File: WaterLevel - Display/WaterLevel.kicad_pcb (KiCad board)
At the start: 2 copper layers, 58 parts, among them P1 PWR_SW, P2 PROBE, P3 AC 12V, P4 PUMP, P5 ALARM, Q1 2N2222, Q2 2N2222, U1 LM324N, U2 LM7812CT, U3 LM324N, U4 LM324N

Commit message: Display
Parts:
- removed C1: CP, Capacitors_ThroughHole:C_Radial_D5_L11_P2.5
- removed C2: CP, Capacitors_ThroughHole:C_Axial_D13_L31_P38
- removed D10: LN1, LEDs:LED-5MM
- removed D11: LN2, LEDs:LED-5MM
- removed D12: LN3, LEDs:LED-5MM
- removed D13: LN4, LEDs:LED-5MM
- removed D14: LN5, LEDs:LED-5MM
- removed D15: LN6, LEDs:LED-5MM
- removed D16: LN7, LEDs:LED-5MM
- removed D17: LN8, LEDs:LED-5MM
- removed D9: ALRM_LED, LEDs:LED-5MM
- removed F1: FUSE, Fuse_Holders_and_Fuses:Fuseholder5x20_horiz_open_Schurter_0031_8201
- removed P2: PROBE, Sockets_MOLEX_KK-System:Socket_MOLEX-KK-RM3-96mm_Lock_3pin_straight
- removed P3: AC 12V, Sockets_MOLEX_KK-System:Socket_MOLEX-KK-RM3-96mm_Lock_2pin_straight
- removed P4: PUMP, Sockets_MOLEX_KK-System:Socket_MOLEX-KK-RM3-96mm_Lock_2pin_straight
- removed P5: ALARM, Sockets_MOLEX_KK-System:Socket_MOLEX-KK-RM3-96mm_Lock_3pin_straight
- removed Q1, Q2: 2N2222, TO_SOT_Packages_THT:TO-18_3Pin
- removed R16, R17, R18, R19, R20: R, Resistors_ThroughHole:Resistor_Horizontal_RM7mm
- removed RL1, RL2: 12V/2A, Relays_ThroughHole:Relay_SPDT_Schrack-RT1_RM5mm
- removed RV3: ALRM_LVL, Potentiometers:Potentiometer_Trimmer-Piher_PT15-V15_horizontal
- removed RV4: LVL, Potentiometers:Potentiometer_Trimmer-Piher_PT15-V15_horizontal
- removed RV5: LVH, Potentiometers:Potentiometer_Trimmer-Piher_PT15-V15_horizontal
- removed U3, U4: LM324N, Housings_DIP:DIP-14_W7.62mm_LongPads
- D1: value 1N4007 -> LN1; footprint Diodes_ThroughHole:Diode_DO-41_SOD81_Vertical_KathodeUp -> LEDs:LED-5MM
- D2: value PUMP_LED -> LN2
- D3: value D -> LN3; footprint Diodes_ThroughHole:Diode_DO-41_SOD81_Vertical_KathodeUp -> LEDs:LED-5MM
- D4: value D -> LN4; footprint Diodes_ThroughHole:Diode_DO-41_SOD81_Vertical_KathodeUp -> LEDs:LED-5MM
- D5: value D -> LN5; footprint Diodes_ThroughHole:Diode_DO-41_SOD81_Vertical_KathodeUp -> LEDs:LED-5MM
- D6: value D -> LN6; footprint Diodes_ThroughHole:Diode_DO-41_SOD81_Vertical_KathodeUp -> LEDs:LED-5MM
- D7: value PWR_LED -> LN7
- D8: value 1N4007 -> LN8; footprint Diodes_ThroughHole:Diode_DO-41_SOD81_Vertical_KathodeUp -> LEDs:LED-5MM
- P1: value PWR_SW -> DISPLAY; footprint Sockets_MOLEX_KK-System:Socket_MOLEX-KK-RM3-96mm_Lock_2pin_straight -> Sockets_MOLEX_KK-System:Socket_MOLEX-KK-RM2-54mm_Lock_3pin_straight
- RV1: value POT -> LVL
- RV2: value POT -> LVH
- U2: value LM7812CT -> LM324N; footprint Power_Integrations:TO-220 -> Housings_DIP:DIP-14_W7.62mm_LongPads
- moved D6 117.4 mm to (151.9, 148.8), turned to 270 degrees
- moved D5 109.5 mm to (145.8, 148.8), turned to 270 degrees
- moved D1 106.5 mm to (120.9, 148.8)
- moved P1 100.1 mm to (162.1, 115.6), turned to 90 degrees
- moved D2 99.4 mm to (127.5, 148.8), turned to 270 degrees
- moved D4 98.4 mm to (139.7, 148.8), turned to 270 degrees
- moved R1 95.1 mm to (118.6, 131.6), turned to 180 degrees
- moved D3 90.4 mm to (133.6, 148.8), turned to 270 degrees
- moved R6 83.3 mm to (156.7, 128.5), turned to 180 degrees
- moved D7 78.8 mm to (158.0, 148.8), turned to 270 degrees
- moved R13 77.2 mm to (151.9, 137.9)
- moved R14 76.9 mm to (158.0, 137.9)
- moved R15 76.7 mm to (164.1, 137.9)
- moved R3 71.9 mm to (133.9, 131.6), turned to 180 degrees
- moved RV1 69.2 mm to (104.4, 151.4), turned to 0 degrees
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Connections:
- D1 pad 1: +12V -> Net-(D1-Pad1)
- D1 pad 2: Net-(D1-Pad2) -> +12V
- D2 pad 1: Net-(D1-Pad2) -> Net-(D2-Pad1)
- D2 pad 2: Net-(D2-Pad2) -> +12V
- D3 pad 2: Net-(D3-Pad2) -> +12V
- D4 pad 1: Net-(D3-Pad1) -> Net-(D4-Pad1)
- D4 pad 2: Net-(D4-Pad2) -> +12V
- D5 pad 1: GNDPWR -> Net-(D5-Pad1)
- D5 pad 2: Net-(D3-Pad2) -> +12V
- D6 pad 1: GNDPWR -> Net-(D6-Pad1)
- D6 pad 2: Net-(D4-Pad2) -> +12V
- D7 pad 1: GNDPWR -> Net-(D7-Pad1)
- D7 pad 2: Net-(D7-Pad2) -> +12V
- D8 pad 1: +12V -> Net-(D8-Pad1)
- D8 pad 2: Net-(D8-Pad2) -> +12V
- P1 pad 1: Net-(D3-Pad1) -> +12V
- P1 pad 2: +12VA -> Net-(P1-Pad2)
- R1 pad 1: +12V -> Net-(R1-Pad1)
- R1 pad 2: Net-(D2-Pad2) -> Net-(R1-Pad2)
- R10 pad 2: Net-(R10-Pad2) -> Net-(D3-Pad1)
- R11 pad 2: Net-(R10-Pad1) -> Net-(D4-Pad1)
- R12 pad 2: Net-(R11-Pad1) -> Net-(D5-Pad1)
- R13 pad 2: Net-(D10-Pad1) -> Net-(D6-Pad1)
- R14 pad 2: Net-(D11-Pad1) -> Net-(D7-Pad1)
- R15 pad 2: Net-(D12-Pad1) -> Net-(D8-Pad1)
- R2 pad 1: +12V -> Net-(R2-Pad1)
- R2 pad 2: Net-(D7-Pad2) -> Net-(R1-Pad1)
- R3 pad 2: Net-(Q1-Pad2) -> Net-(R2-Pad1)
- R4 pad 1: +12V -> Net-(R4-Pad1)
- R4 pad 2: Net-(D9-Pad2) -> Net-(R3-Pad1)
- R5 pad 2: Net-(Q2-Pad2) -> Net-(R4-Pad1)
- R6 pad 2: Net-(R6-Pad2) -> Net-(R5-Pad1)
- R8 pad 2: Net-(R7-Pad1) -> Net-(D1-Pad1)
- R9 pad 1: Net-(R10-Pad2) -> Net-(R9-Pad1)
- R9 pad 2: Net-(R8-Pad1) -> Net-(D2-Pad1)
- RV1 pad 1: +12V -> Net-(R1-Pad2)
- RV1 pad 2: Net-(RV1-Pad2) -> Net-(R1-Pad2)
- RV2 pad 1: VProbe -> +12V
- RV2 pad 2: Net-(RV2-Pad2) -> +12V
- RV2 pad 3: Net-(R3-Pad1) -> Net-(R7-Pad1)
- U1 pad 1: Net-(R3-Pad1) -> Net-(R8-Pad1)
- U1 pad 10: (no net) -> Net-(R2-Pad1)
- U1 pad 11: GNDPWR -> +12V
- U1 pad 12: (no net) -> Net-(R3-Pad1)
- U1 pad 13: (no net) -> Net-(P1-Pad2)
- U1 pad 14: (no net) -> Net-(R11-Pad1)
- U1 pad 2: Net-(RV1-Pad2) -> Net-(P1-Pad2)
- U1 pad 3: Net-(RV2-Pad2) -> Net-(R1-Pad2)
- U1 pad 4: +12V -> GNDPWR
- U1 pad 5: VProbe -> Net-(R1-Pad1)
- U1 pad 6: Net-(RV3-Pad2) -> Net-(P1-Pad2)
- U1 pad 7: Net-(R5-Pad1) -> Net-(R9-Pad1)
- U1 pad 8: (no net) -> Net-(R10-Pad1)
- U1 pad 9: (no net) -> Net-(P1-Pad2)
- U2 pad 1: +12VA -> Net-(R12-Pad1)
- U2 pad 2: GNDPWR -> Net-(P1-Pad2)
- U2 pad 3: +12V -> Net-(R4-Pad1)
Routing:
- net +12V: track 0.00 -> 169.2 mm
- net GNDPWR: track 0.00 -> 141.8 mm
- net Net-(R1-Pad2): track 0.00 -> 56.1 mm
- net Net-(R11-Pad1): track 0.00 -> 37.8 mm
- net Net-(R10-Pad1): track 0.00 -> 19.5 mm
- net Net-(R9-Pad1): track 0.00 -> 18.4 mm
- net Net-(R2-Pad1): track 0.00 -> 3.56 mm
- net Net-(D8-Pad1): track 0.00 -> 3.30 mm
- net Net-(D7-Pad1): track 0.00 -> 3.30 mm
- net Net-(D6-Pad1): track 0.00 -> 3.30 mm
- net Net-(D5-Pad1): track 0.00 -> 3.30 mm
- net Net-(D4-Pad1): track 0.00 -> 3.30 mm
- net Net-(D3-Pad1): track 0.00 -> 3.30 mm
- net Net-(D2-Pad1): track 0.00 -> 3.30 mm
- net Net-(D1-Pad1): track 0.00 -> 3.30 mm
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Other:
- net class Default: trace_width 0.25 -> 1

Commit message: PCB changes
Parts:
- moved RV2 3.09 mm to (104.4, 121.7)
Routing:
- net Net-(R8-Pad1): track 0.00 -> 37.3 mm, vias 0 -> 2
- net Net-(R12-Pad1): track 0.00 -> 36.5 mm, vias 0 -> 2
- net +12V: track 169.2 -> 202.3 mm
- net Net-(R1-Pad1): track 1.78 -> 24.1 mm, vias 0 -> 2
- net Net-(R3-Pad1): track 3.05 -> 25.2 mm
- net Net-(R4-Pad1): track 3.05 -> 24.9 mm
- net Net-(R14-Pad1): track 0.00 -> 20.8 mm
- net Net-(R13-Pad1): track 0.00 -> 20.8 mm
- net Net-(R2-Pad1): track 3.56 -> 20.4 mm
- net Net-(R5-Pad1): track 3.05 -> 18.5 mm
- net Net-(R6-Pad1): track 3.05 -> 18.4 mm
- net Net-(R11-Pad1): track 37.8 -> 35.6 mm
- net Net-(R9-Pad1): track 18.4 -> 20.5 mm
- net Net-(R1-Pad2): track 56.1 -> 58.0 mm
- net Net-(R10-Pad1): track 19.5 -> 20.1 mm
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
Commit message: Updates
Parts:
- added P2: VIN, Wire_Pads:SolderWirePad_single_1mmDrill, F.Cu at (166.8, 109.5)
- added P3: +12V, Wire_Pads:SolderWirePad_single_1mmDrill, F.Cu at (167.0, 102.0)
- P1: value DISPLAY -> GND; footprint Sockets_MOLEX_KK-System:Socket_MOLEX-KK-RM2-54mm_Lock_3pin_straight -> Wire_Pads:SolderWirePad_single_1mmDrill
- moved P1 5.24 mm to (166.8, 113.2)
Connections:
- P1 pad 1: +12V -> GNDPWR
- U1 pad 13: Net-(P1-Pad2) -> Net-(P2-Pad1)
- U1 pad 2: Net-(P1-Pad2) -> Net-(P2-Pad1)
- U1 pad 6: Net-(P1-Pad2) -> Net-(P2-Pad1)
- U1 pad 9: Net-(P1-Pad2) -> Net-(P2-Pad1)
- U2 pad 13: Net-(P1-Pad2) -> Net-(P2-Pad1)
- U2 pad 2: Net-(P1-Pad2) -> Net-(P2-Pad1)
- U2 pad 6: Net-(P1-Pad2) -> Net-(P2-Pad1)
- U2 pad 9: Net-(P1-Pad2) -> Net-(P2-Pad1)

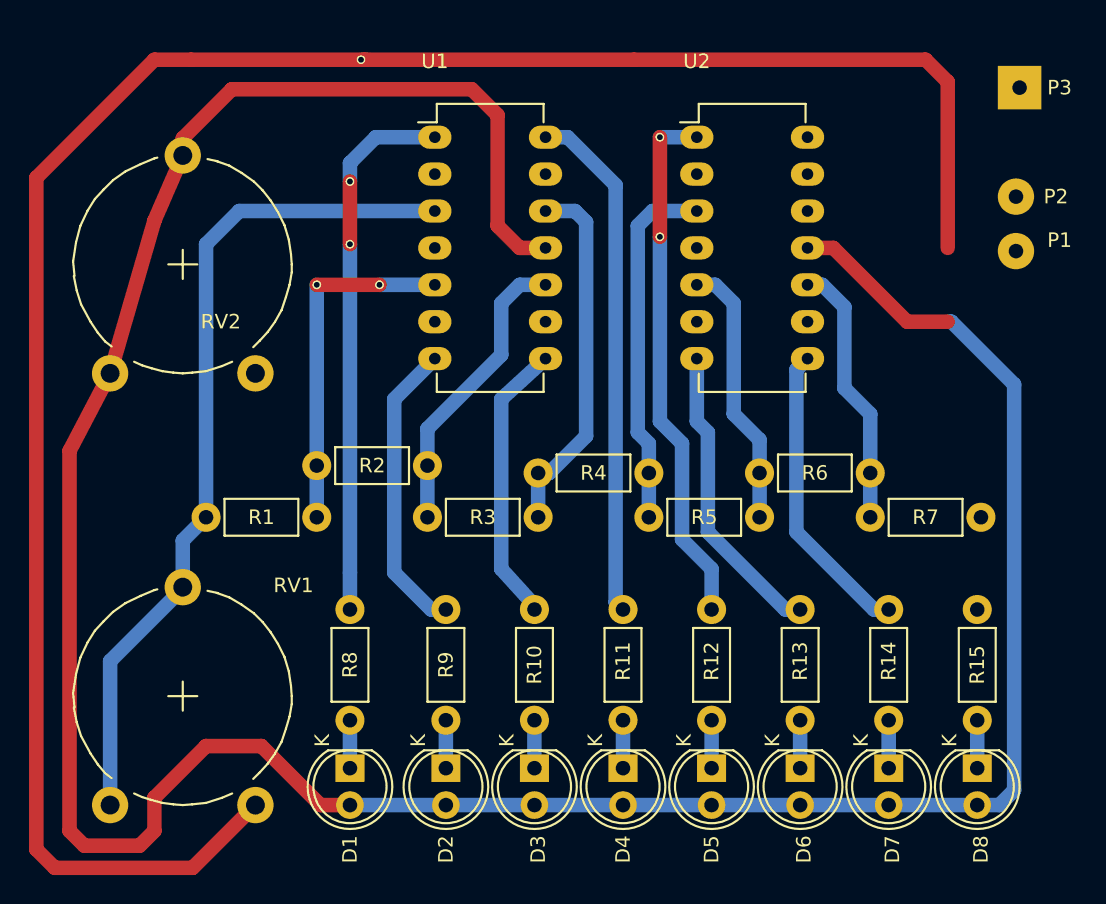
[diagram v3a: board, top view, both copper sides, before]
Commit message: Fixed Sonde Before display test
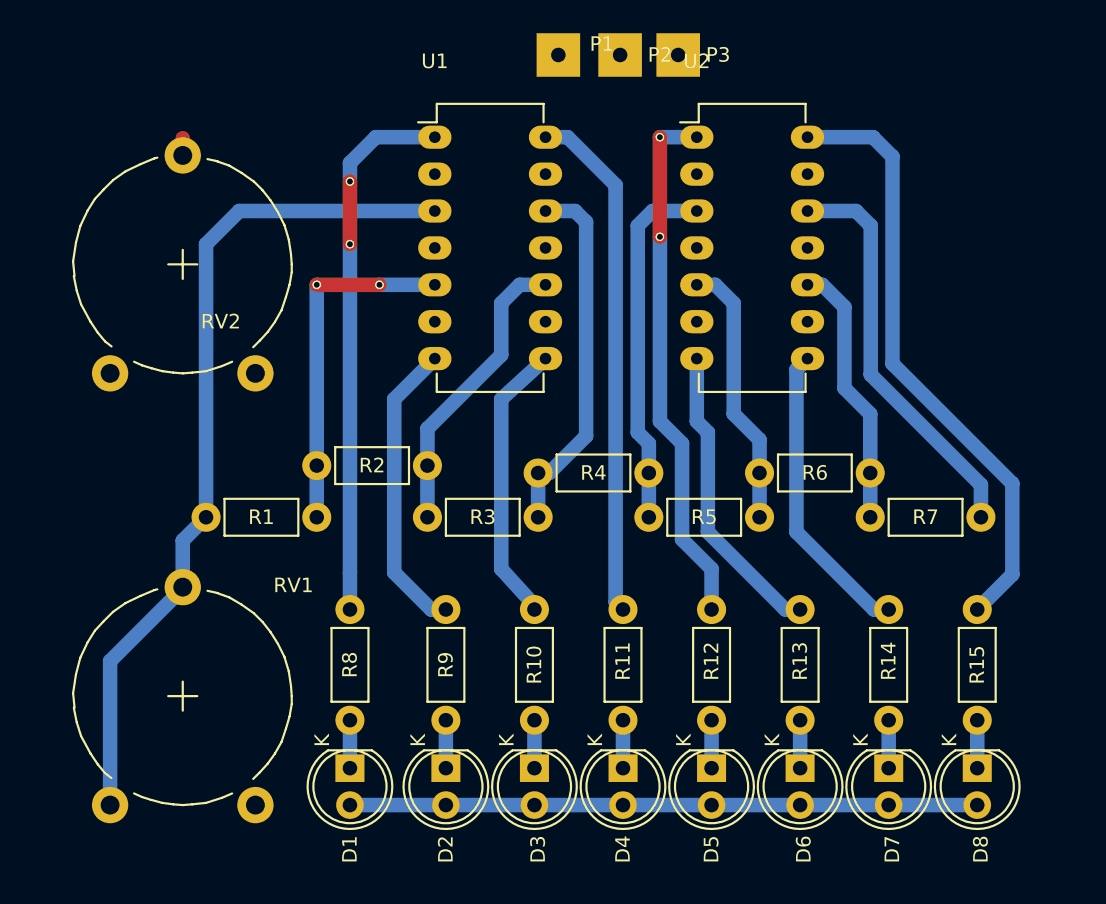
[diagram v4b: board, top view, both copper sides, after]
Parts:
- moved P1 34.3 mm to (135.2, 99.8)
- moved P2 28.9 mm to (139.5, 99.8)
- moved P3 23.6 mm to (143.5, 99.8)
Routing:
- net +12V: track 202.3 -> 44.4 mm
- net GNDPWR: track 142.3 -> 0.00 mm, vias 1 -> 0
- net Net-(R15-Pad1): track 0.00 -> 42.0 mm
- net Net-(R7-Pad1): track 0.00 -> 28.0 mm
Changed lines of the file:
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@@
   (general
     (links 56)
-    (no_connects 16)
-    (area 98.613999 97.315 168.996 156.402002)
+    (no_connects 17)
+    (area 98.613999 99.065 175.275 156.402002)
     (thickness 1.6)
     (drawings 0)
-    (tracks 138)
+    (tracks 110)
     (zones 0)
     (modules 30)
@@
   )
   (module Wire_Pads:SolderWirePad_single_1mmDrill (layer F.Cu)
-    (at 166.75 113.25 90)
+    (at 135.25 99.75 90)
     (fp_text reference P1 (at 0.75 3 180) (layer F.SilkS)
       (effects (font (size 1 1) (thickness 0.15)))
@@
       (effects (font (size 1 1) (thickness 0.15)))
     )
-    (pad 1 thru_hole circle (at 0 0 90) (size 2.49936 2.49936) (drill 1.00076) (layers *.Cu *.Mask F.SilkS)
+    (pad 1 thru_hole rect (at 0 0 90) (size 3 3) (drill 1.00076) (layers *.Cu *.Mask F.SilkS)
       (net 2 GNDPWR))
   )
   (module Wire_Pads:SolderWirePad_single_1mmDrill (layer F.Cu)
-    (at 166.75 109.5)
+    (at 139.5 99.75)
     (fp_text reference P2 (at 2.75 0) (layer F.SilkS)
       (effects (font (size 1 1) (thickness 0.15)))
@@
       (effects (font (size 1 1) (thickness 0.15)))
     )
-    (pad 1 thru_hole circle (at 0 0) (size 2.49936 2.49936) (drill 1.00076) (layers *.Cu *.Mask F.SilkS)
+    (pad 1 thru_hole rect (at 0 0) (size 3 3) (drill 1.00076) (layers *.Cu *.Mask F.SilkS)
       (net 27 "Net-(P2-Pad1)"))
   )
   (module Wire_Pads:SolderWirePad_single_1mmDrill (layer F.Cu)
-    (at 167 102)
+    (at 143.5 99.75)
     (fp_text reference P3 (at 2.75 0) (layer F.SilkS)
       (effects (font (size 1 1) (thickness 0.15)))
@@
       (net 1 +12V))
   )
-  (segment (start 162.052 118.11) (end 162.306 118.11) (width 1) (layer B.Cu) (net 1))
-  (segment (start 162.306 118.11) (end 166.624 122.428) (width 1) (layer B.Cu) (net 1))
-  (segment (start 165.608 151.384) (end 164.084 151.384) (width 1) (layer B.Cu) (net 1))
-  (segment (start 166.624 150.368) (end 165.608 151.384) (width 1) (layer B.Cu) (net 1))
-  (segment (start 166.624 122.428) (end 166.624 150.368) (width 1) (layer B.Cu) (net 1))
   (segment (start 120.904 151.384) (end 127.508 151.384) (width 1) (layer B.Cu) (net 1))
   (segment (start 127.508 151.384) (end 133.604 151.384) (width 1) (layer B.Cu) (net 1))
@@
   (segment (start 164.084 151.384) (end 157.988 151.384) (width 1) (layer B.Cu) (net 1))
   (segment (start 109.39526 106.66476) (end 109.39526 105.48874) (width 1) (layer F.Cu) (net 1))
-  (segment (start 109.39526 105.48874) (end 112.776 102.108) (width 1) (layer F.Cu) (net 1))
-  (segment (start 132.588 113.03) (end 134.366 113.03) (width 1) (layer F.Cu) (net 1))
-  (segment (start 131.064 111.506) (end 132.588 113.03) (width 1) (layer F.Cu) (net 1))
-  (segment (start 131.064 103.886) (end 131.064 111.506) (width 1) (layer F.Cu) (net 1))
-  (segment (start 129.286 102.108) (end 131.064 103.886) (width 1) (layer F.Cu) (net 1))
-  (segment (start 112.776 102.108) (end 129.286 102.108) (width 1) (layer F.Cu) (net 1))
-  (segment (start 120.904 151.384) (end 118.872 151.384) (width 1) (layer F.Cu) (net 1))
-  (segment (start 101.6 127) (end 104.394 121.666) (width 1) (layer F.Cu) (net 1) (status 20))
-  (segment (start 101.6 153.162) (end 101.6 127) (width 1) (layer F.Cu) (net 1))
-  (segment (start 102.616 154.178) (end 101.6 153.162) (width 1) (layer F.Cu) (net 1))
-  (segment (start 106.426 154.178) (end 102.616 154.178) (width 1) (layer F.Cu) (net 1))
-  (segment (start 107.442 153.162) (end 106.426 154.178) (width 1) (layer F.Cu) (net 1))
-  (segment (start 107.442 150.876) (end 107.442 153.162) (width 1) (layer F.Cu) (net 1))
-  (segment (start 110.998 147.32) (end 107.442 150.876) (width 1) (layer F.Cu) (net 1))
-  (segment (start 114.808 147.32) (end 110.998 147.32) (width 1) (layer F.Cu) (net 1))
-  (segment (start 118.872 151.384) (end 114.808 147.32) (width 1) (layer F.Cu) (net 1))
-  (segment (start 152.4 113.03) (end 154.178 113.03) (width 1) (layer F.Cu) (net 1))
-  (segment (start 159.258 118.11) (end 162.052 118.11) (width 1) (layer F.Cu) (net 1))
-  (segment (start 154.178 113.03) (end 159.258 118.11) (width 1) (layer F.Cu) (net 1))
-  (segment (start 104.394 121.666) (end 107.442 111.15802) (width 1) (layer F.Cu) (net 1) (status 10))
-  (segment (start 107.442 111.15802) (end 109.39526 106.66476) (width 1) (layer F.Cu) (net 1) (status 20))
-  (via (at 121.666 100.076) (size 0.6) (drill 0.4) (layers F.Cu B.Cu) (net 2))
-  (segment (start 122.174 100.076) (end 121.666 100.076) (width 1) (layer B.Cu) (net 2))
-  (segment (start 109.982 100.076) (end 107.442 100.076) (width 1) (layer F.Cu) (net 2))
-  (segment (start 162.052 101.6) (end 160.528 100.076) (width 1) (layer F.Cu) (net 2))
-  (segment (start 160.528 100.076) (end 140.462 100.076) (width 1) (layer F.Cu) (net 2))
-  (segment (start 140.462 100.076) (end 121.92 100.076) (width 1) (layer F.Cu) (net 2))
-  (segment (start 121.92 100.076) (end 109.982 100.076) (width 1) (layer F.Cu) (net 2))
-  (segment (start 162.052 113.03) (end 162.052 101.6) (width 1) (layer F.Cu) (net 2))
-  (segment (start 110.07852 155.702) (end 114.39652 151.384) (width 1) (layer F.Cu) (net 2))
-  (segment (start 100.584 155.702) (end 110.07852 155.702) (width 1) (layer F.Cu) (net 2))
-  (segment (start 99.314 154.432) (end 100.584 155.702) (width 1) (layer F.Cu) (net 2))
-  (segment (start 99.314 108.204) (end 99.314 154.432) (width 1) (layer F.Cu) (net 2))
-  (segment (start 107.442 100.076) (end 99.314 108.204) (width 1) (layer F.Cu) (net 2))
   (segment (start 133.604 148.844) (end 133.604 145.542) (width 1) (layer B.Cu) (net 3))
   (segment (start 133.858 128.524) (end 134.62 128.524) (width 1) (layer B.Cu) (net 4))
@@
   (segment (start 153.416 115.57) (end 152.4 115.57) (width 1) (layer B.Cu) (net 6))
   (segment (start 156.718 131.572) (end 156.718 128.524) (width 1) (layer B.Cu) (net 6))
+  (segment (start 152.4 110.49) (end 155.74 110.49) (width 1) (layer B.Cu) (net 7) (status 400000))
+  (segment (start 164.338 129.338) (end 164.338 131.572) (width 1) (layer B.Cu) (net 7) (status 800000))
+  (segment (start 156.75 121.75) (end 164.338 129.338) (width 1) (layer B.Cu) (net 7))
+  (segment (start 156.75 111.5) (end 156.75 121.75) (width 1) (layer B.Cu) (net 7))
+  (segment (start 155.74 110.49) (end 156.75 111.5) (width 1) (layer B.Cu) (net 7))
+  (segment (start 120.904 108.458) (end 120.904 112.776) (width 1) (layer F.Cu) (net 8))
   (segment (start 126.746 105.41) (end 122.682 105.41) (width 1) (layer B.Cu) (net 8))
   (segment (start 120.904 135.382) (end 120.904 112.776) (width 1) (layer B.Cu) (net 8))
   (via (at 120.904 112.776) (size 0.6) (drill 0.4) (layers F.Cu B.Cu) (net 8))
   (segment (start 120.904 135.382) (end 120.904 137.922) (width 1) (layer B.Cu) (net 8))
-  (segment (start 120.904 108.458) (end 120.904 112.776) (width 1) (layer F.Cu) (net 8))
   (via (at 120.904 108.458) (size 0.6) (drill 0.4) (layers F.Cu B.Cu) (net 8))
   (segment (start 120.904 107.188) (end 120.904 108.458) (width 1) (layer B.Cu) (net 8))
@@
   (segment (start 151.638 132.588) (end 151.638 121.412) (width 1) (layer B.Cu) (net 13))
   (segment (start 156.972 137.922) (end 151.638 132.588) (width 1) (layer B.Cu) (net 13))
+  (segment (start 152.4 105.41) (end 156.91 105.41) (width 1) (layer B.Cu) (net 14) (status 400000))
+  (segment (start 166.5 135.506) (end 164.084 137.922) (width 1) (layer B.Cu) (net 14) (status 800000))
+  (segment (start 166.5 129.25) (end 166.5 135.506) (width 1) (layer B.Cu) (net 14))
+  (segment (start 158.25 121) (end 166.5 129.25) (width 1) (layer B.Cu) (net 14))
+  (segment (start 158.25 106.75) (end 158.25 121) (width 1) (layer B.Cu) (net 14))
+  (segment (start 156.91 105.41) (end 158.25 106.75) (width 1) (layer B.Cu) (net 14))
   (segment (start 120.904 148.844) (end 120.904 145.542) (width 1) (layer B.Cu) (net 15))
   (segment (start 127.508 148.844) (end 127.508 145.542) (width 1) (layer B.Cu) (net 16))
